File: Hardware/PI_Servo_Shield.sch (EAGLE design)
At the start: 58 parts, among them J1 RASPBERRYPI-40-PIN-GPIO, J19 QWIIC, J20 USB C, J21 Serial, U1 PCA9685, U2 PCA9306, U3 CH340C

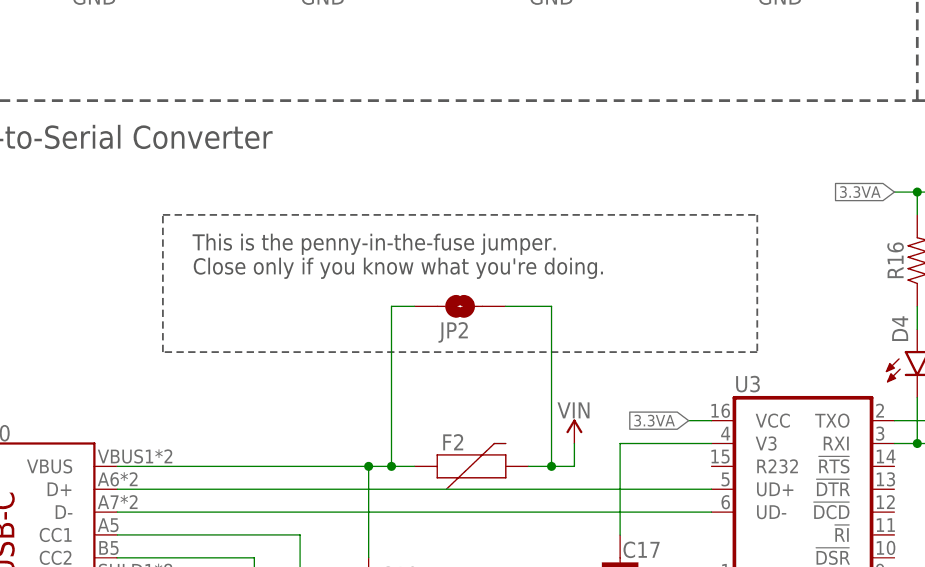
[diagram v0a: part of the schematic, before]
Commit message: adjusted I2C pullup and label
modified sch note for bypass fuse jumper
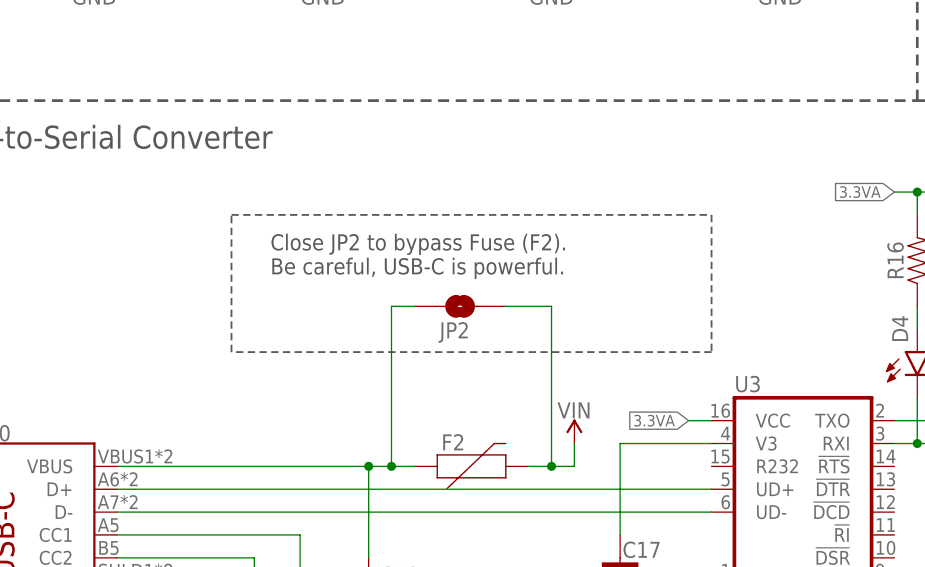
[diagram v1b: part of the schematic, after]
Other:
- note added: "Close JP2 to bypass Fuse (F2). Be careful, USB-C is powerful."
- note removed: "This is the penny-in-the-fuse jumper. Close only if you know what you're doing."
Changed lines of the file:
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@@
 <grid distance="0.1" unitdist="inch" unit="inch" style="lines" multiple="1" display="no" altdistance="0.01" altunitdist="inch" altunit="inch"/>
 <layers>
-<layer number="1" name="Top" color="4" fill="1" visible="yes" active="no"/>
-<layer number="2" name="Route2" color="1" fill="3" visible="yes" active="no"/>
-<layer number="3" name="Route3" color="4" fill="3" visible="yes" active="no"/>
-<layer number="4" name="Route4" color="1" fill="4" visible="yes" active="no"/>
-<layer number="5" name="Route5" color="4" fill="4" visible="yes" active="no"/>
-<layer number="6" name="Route6" color="1" fill="8" visible="yes" active="no"/>
-<layer number="7" name="Route7" color="4" fill="8" visible="yes" active="no"/>
-<layer number="8" name="Route8" color="1" fill="2" visible="yes" active="no"/>
-<layer number="9" name="Route9" color="4" fill="2" visible="yes" active="no"/>
-<layer number="10" name="Route10" color="1" fill="7" visible="yes" active="no"/>
-<layer number="11" name="Route11" color="4" fill="7" visible="yes" active="no"/>
-<layer number="12" name="Route12" color="1" fill="5" visible="yes" active="no"/>
-<layer number="13" name="Route13" color="4" fill="5" visible="yes" active="no"/>
-<layer number="14" name="Route14" color="1" fill="6" visible="yes" active="no"/>
-<layer number="15" name="Route15" color="4" fill="6" visible="yes" active="no"/>
-<layer number="16" name="Bottom" color="1" fill="1" visible="yes" active="no"/>
-<layer number="17" name="Pads" color="2" fill="1" visible="yes" active="no"/>
-<layer number="18" name="Vias" color="2" fill="1" visible="yes" active="no"/>
-<layer number="19" name="Unrouted" color="6" fill="1" visible="yes" active="no"/>
-<layer number="20" name="Dimension" color="15" fill="1" visible="yes" active="no"/>
-<layer number="21" name="tPlace" color="16" fill="1" visible="yes" active="no"/>
-<layer number="22" name="bPlace" color="14" fill="1" visible="yes" active="no"/>
-<layer number="23" name="tOrigins" color="15" fill="1" visible="yes" active="no"/>
-<layer number="24" name="bOrigins" color="15" fill="1" visible="yes" active="no"/>
-<layer number="25" name="tNames" color="7" fill="1" visible="yes" active="no"/>
-<layer number="26" name="bNames" color="7" fill="1" visible="yes" active="no"/>
-<layer number="27" name="tValues" color="7" fill="1" visible="yes" active="no"/>
-<layer number="28" name="bValues" color="7" fill="1" visible="yes" active="no"/>
+<layer number="1" name="Top" color="4" fill="1" visible="no" active="no"/>
+<layer number="2" name="Route2" color="1" fill="3" visible="no" active="no"/>
+<layer number="3" name="Route3" color="4" fill="3" visible="no" active="no"/>
+<layer number="4" name="Route4" color="1" fill="4" visible="no" active="no"/>
+<layer number="5" name="Route5" color="4" fill="4" visible="no" active="no"/>
+<layer number="6" name="Route6" color="1" fill="8" visible="no" active="no"/>
+<layer number="7" name="Route7" color="4" fill="8" visible="no" active="no"/>
+<layer number="8" name="Route8" color="1" fill="2" visible="no" active="no"/>
+<layer number="9" name="Route9" color="4" fill="2" visible="no" active="no"/>
+<layer number="10" name="Route10" color="1" fill="7" visible="no" active="no"/>
+<layer number="11" name="Route11" color="4" fill="7" visible="no" active="no"/>
+<layer number="12" name="Route12" color="1" fill="5" visible="no" active="no"/>
+<layer number="13" name="Route13" color="4" fill="5" visible="no" active="no"/>
+<layer number="14" name="Route14" color="1" fill="6" visible="no" active="no"/>
+<layer number="15" name="Route15" color="4" fill="6" visible="no" active="no"/>
+<layer number="16" name="Bottom" color="1" fill="1" visible="no" active="no"/>
+<layer number="17" name="Pads" color="2" fill="1" visible="no" active="no"/>
+<layer number="18" name="Vias" color="2" fill="1" visible="no" active="no"/>
+<layer number="19" name="Unrouted" color="6" fill="1" visible="no" active="no"/>
+<layer number="20" name="Dimension" color="15" fill="1" visible="no" active="no"/>
+<layer number="21" name="tPlace" color="16" fill="1" visible="no" active="no"/>
+<layer number="22" name="bPlace" color="14" fill="1" visible="no" active="no"/>
+<layer number="23" name="tOrigins" color="15" fill="1" visible="no" active="no"/>
+<layer number="24" name="bOrigins" color="15" fill="1" visible="no" active="no"/>
+<layer number="25" name="tNames" color="7" fill="1" visible="no" active="no"/>
+<layer number="26" name="bNames" color="7" fill="1" visible="no" active="no"/>
+<layer number="27" name="tValues" color="7" fill="1" visible="no" active="no"/>
+<layer number="28" name="bValues" color="7" fill="1" visible="no" active="no"/>
 <layer number="29" name="tStop" color="7" fill="3" visible="no" active="no"/>
 <layer number="30" name="bStop" color="7" fill="6" visible="no" active="no"/>
@@
 <layer number="35" name="tGlue" color="7" fill="4" visible="no" active="no"/>
 <layer number="36" name="bGlue" color="7" fill="5" visible="no" active="no"/>
-<layer number="37" name="tTest" color="7" fill="1" visible="yes" active="no"/>
-<layer number="38" name="bTest" color="7" fill="1" visible="yes" active="no"/>
+<layer number="37" name="tTest" color="7" fill="1" visible="no" active="no"/>
+<layer number="38" name="bTest" color="7" fill="1" visible="no" active="no"/>
 <layer number="39" name="tKeepout" color="4" fill="11" visible="no" active="no"/>
 <layer number="40" name="bKeepout" color="1" fill="11" visible="no" active="no"/>
@@
 <layer number="44" name="Drills" color="7" fill="1" visible="no" active="no"/>
 <layer number="45" name="Holes" color="7" fill="1" visible="no" active="no"/>
-<layer number="46" name="Milling" color="3" fill="1" visible="yes" active="no"/>
-<layer number="47" name="Measures" color="7" fill="1" visible="yes" active="no"/>
-<layer number="48" name="Document" color="7" fill="1" visible="yes" active="no"/>
-<layer number="49" name="Reference" color="7" fill="1" visible="yes" active="no"/>
-<layer number="50" name="dxf" color="7" fill="1" visible="yes" active="no"/>
-<layer number="51" name="tDocu" color="6" fill="1" visible="yes" active="no"/>
-<layer number="52" name="bDocu" color="7" fill="1" visible="yes" active="no"/>
-<layer number="53" name="tGND_GNDA" color="7" fill="9" visible="yes" active="no"/>
-<layer number="54" name="bGND_GNDA" color="1" fill="9" visible="yes" active="no"/>
-<layer number="56" name="wert" color="7" fill="1" visible="yes" active="no"/>
-<layer number="57" name="tCAD" color="7" fill="1" visible="yes" active="no"/>
-<layer number="59" name="tCarbon" color="7" fill="1" visible="yes" active="no"/>
-<layer number="60" name="bCarbon" color="7" fill="1" visible="yes" active="no"/>
+<layer number="46" name="Milling" color="3" fill="1" visible="no" active="no"/>
+<layer number="47" name="Measures" color="7" fill="1" visible="no" active="no"/>
+<layer number="48" name="Document" color="7" fill="1" visible="no" active="no"/>
+<layer number="49" name="Reference" color="7" fill="1" visible="no" active="no"/>
+<layer number="50" name="dxf" color="7" fill="1" visible="no" active="no"/>
+<layer number="51" name="tDocu" color="6" fill="1" visible="no" active="no"/>
+<layer number="52" name="bDocu" color="7" fill="1" visible="no" active="no"/>
+<layer number="53" name="tGND_GNDA" color="7" fill="9" visible="no" active="no"/>
+<layer number="54" name="bGND_GNDA" color="1" fill="9" visible="no" active="no"/>
+<layer number="56" name="wert" color="7" fill="1" visible="no" active="no"/>
+<layer number="57" name="tCAD" color="7" fill="1" visible="no" active="no"/>
+<layer number="59" name="tCarbon" color="7" fill="1" visible="no" active="no"/>
+<layer number="60" name="bCarbon" color="7" fill="1" visible="no" active="no"/>
 <layer number="88" name="SimResults" color="9" fill="1" visible="no" active="yes"/>
 <layer number="89" name="SimProbes" color="9" fill="1" visible="no" active="yes"/>
@@
 <text x="174.498" y="6.858" size="2.54" layer="94" font="vector">Pete Lewis</text>
 <text x="2.794" y="96.266" size="2.54" layer="97" font="vector">USB-to-Serial Converter</text>
-<text x="31.242" y="82.296" size="1.778" layer="97" font="vector">This is the penny-in-the-fuse jumper.
-Close only if you know what you're doing.</text>
-<wire x1="93.98" y1="73.66" x2="27.94" y2="73.66" width="0.2032" layer="97" style="shortdash"/>
-<wire x1="27.94" y1="73.66" x2="27.94" y2="88.9" width="0.2032" layer="97" style="shortdash"/>
-<wire x1="27.94" y1="88.9" x2="93.98" y2="88.9" width="0.2032" layer="97" style="shortdash"/>
-<wire x1="93.98" y1="88.9" x2="93.98" y2="73.66" width="0.2032" layer="97" style="shortdash"/>
+<text x="39.878" y="82.296" size="1.778" layer="97" font="vector">Close JP2 to bypass Fuse (F2).
+Be careful, USB-C is powerful.</text>
+<wire x1="88.9" y1="73.66" x2="35.56" y2="73.66" width="0.2032" layer="97" style="shortdash"/>
+<wire x1="35.56" y1="73.66" x2="35.56" y2="88.9" width="0.2032" layer="97" style="shortdash"/>
+<wire x1="35.56" y1="88.9" x2="88.9" y2="88.9" width="0.2032" layer="97" style="shortdash"/>
+<wire x1="88.9" y1="88.9" x2="88.9" y2="73.66" width="0.2032" layer="97" style="shortdash"/>
 <wire x1="210.82" y1="116.84" x2="210.82" y2="35.56" width="0.3048" layer="97" style="longdash"/>
 </plain>

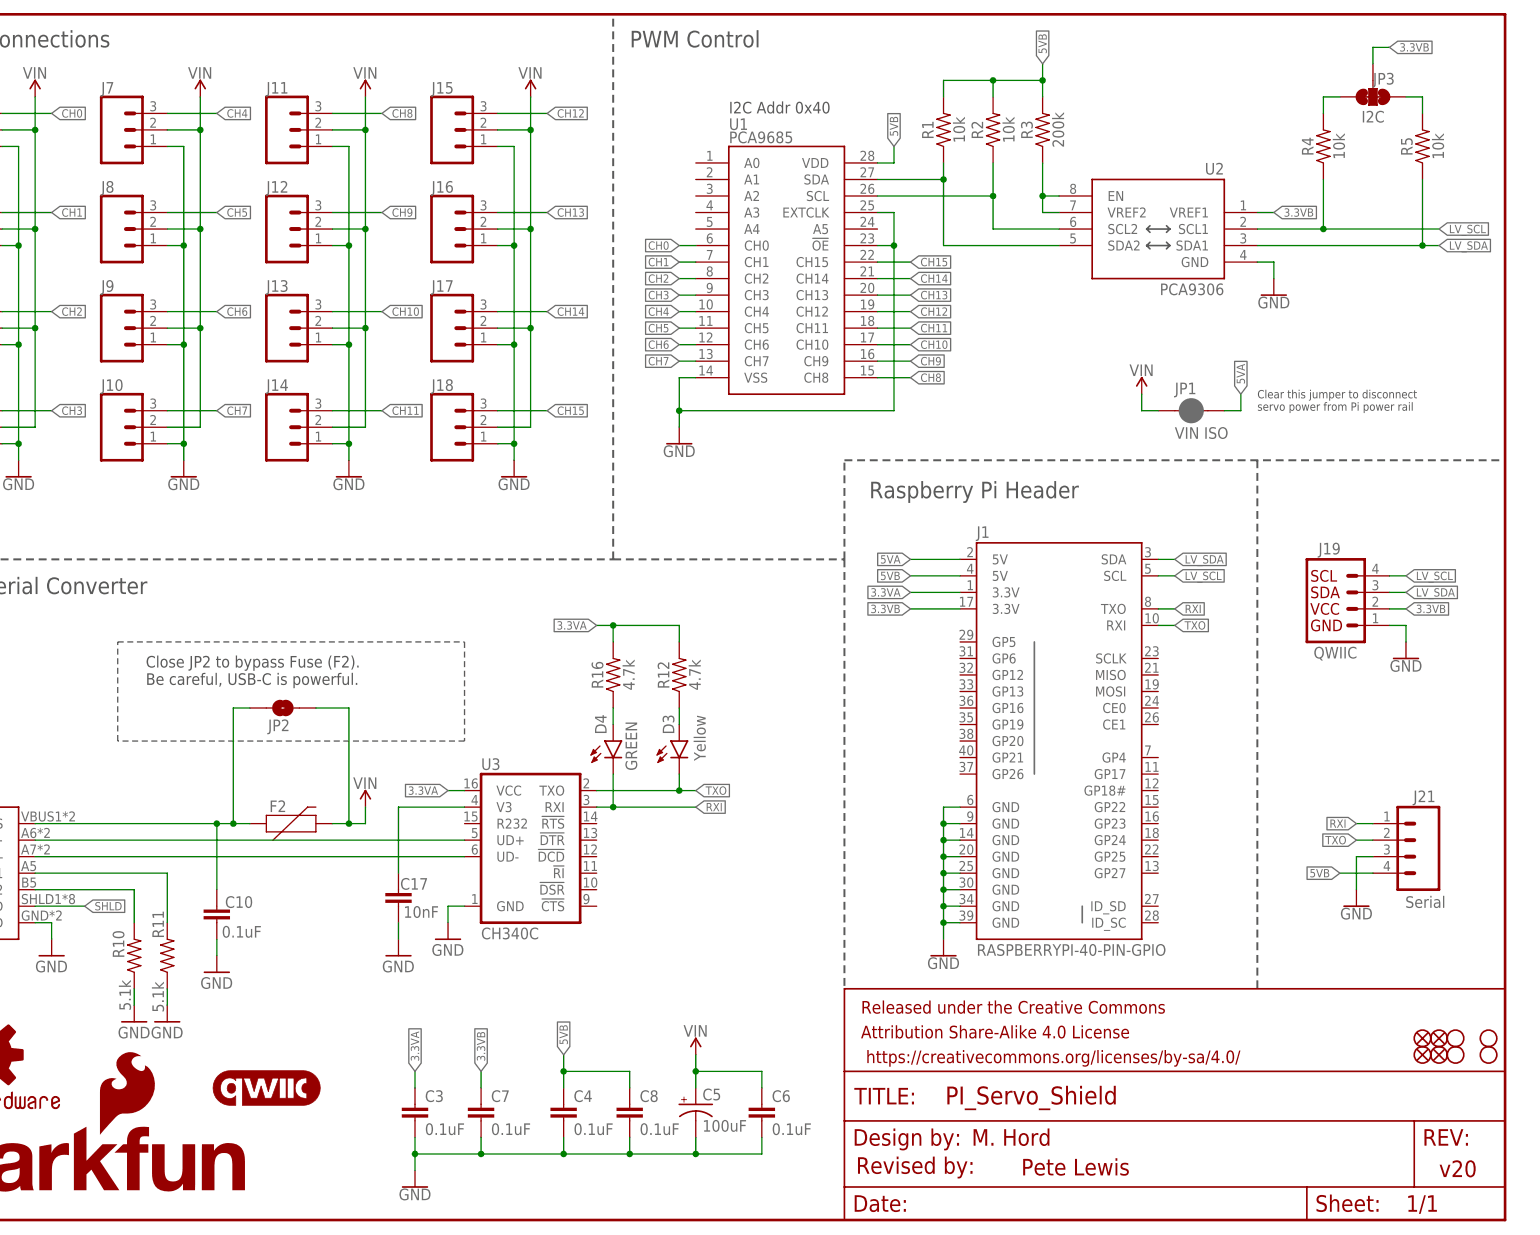
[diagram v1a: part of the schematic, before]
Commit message: post proto-design-review
SCH cleanup:
-3.3VA and 3.3VB combined into a single net and changed to arrow power symbol
-5VA and 5VB combined into a single net and changed to arrow power symbol
-added note about serial connector mating with sphero RVR
-version to v11, will jump to v20 when going to reds

BRD:
-VIN ISO juper to trace closed.
-Product Name silk updated to include "V2"
-changed "PWR" servo rail labels to "5V"
-corrected RX/TX swap, updated silk to RXI and TXO
-JP2 label changed to "FUSE BP"
-Increased 5V trace to 35 mils on connection from RVR serial header to Pi 5V pins.
-changed version in copper to v11
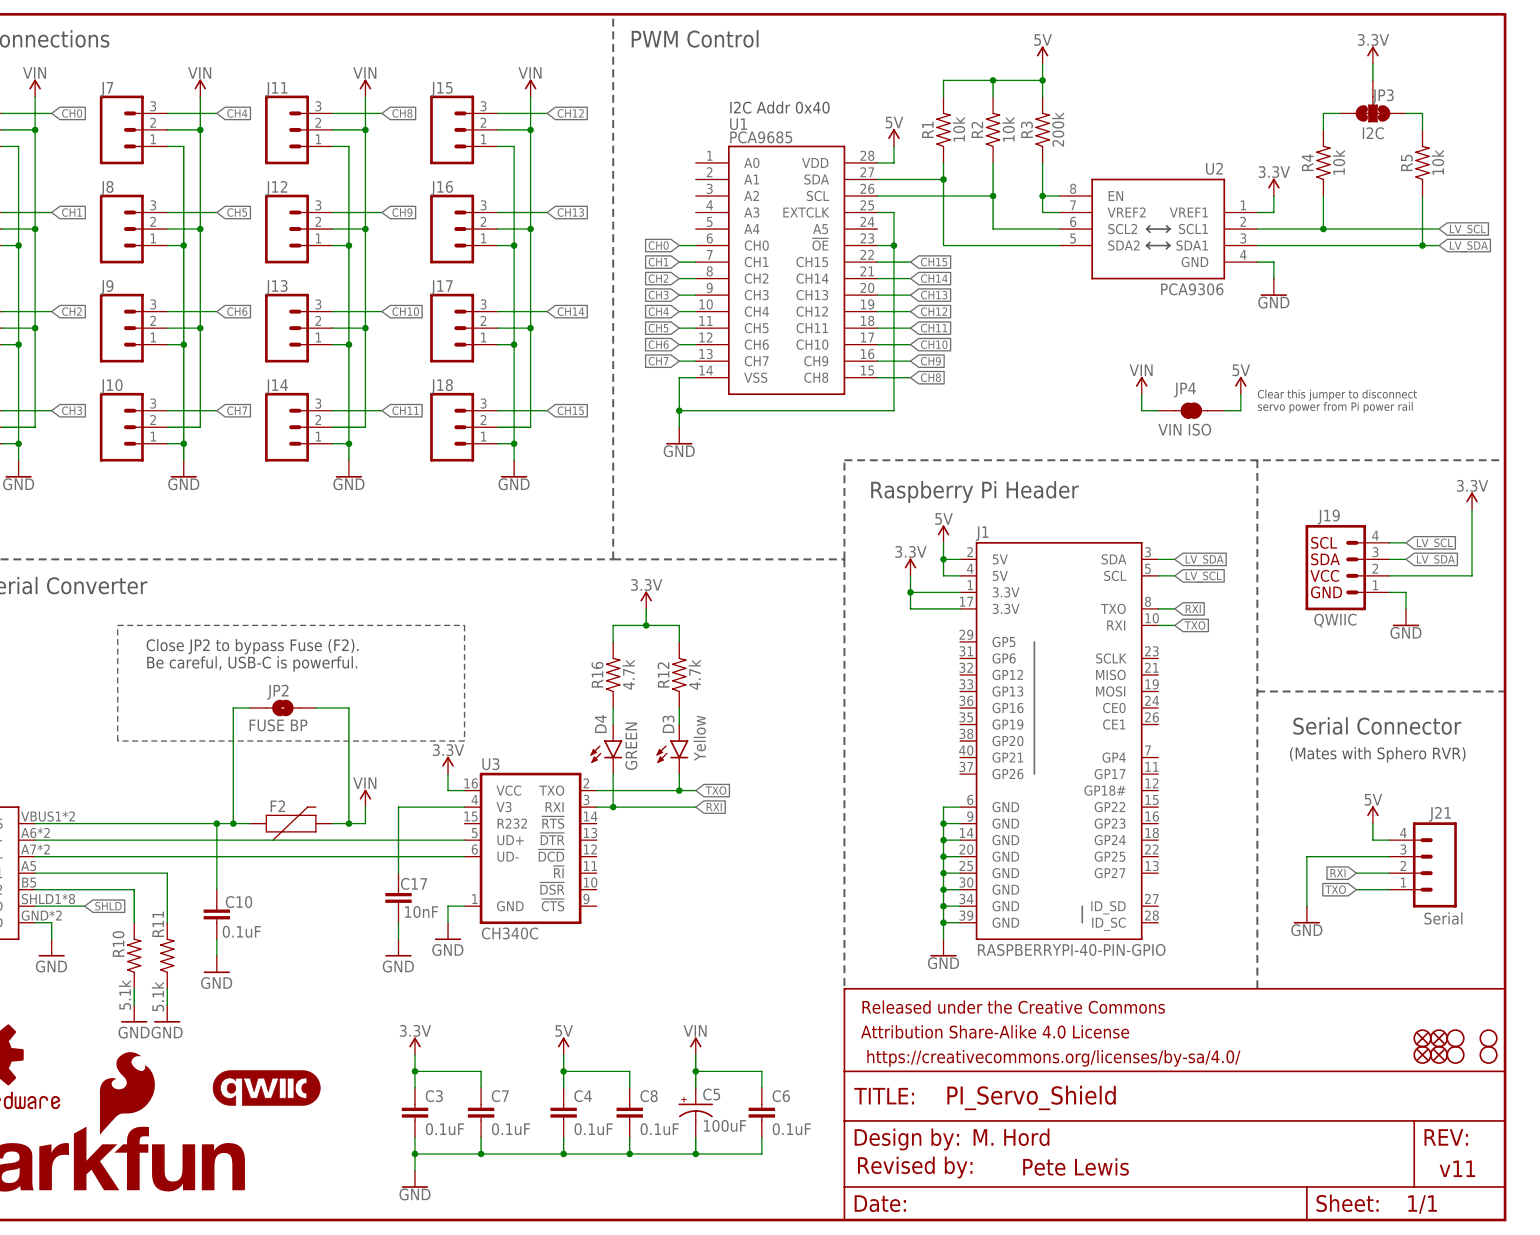
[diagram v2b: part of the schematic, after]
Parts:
- removed JP1: VIN ISO, SparkFun-Jumpers:JUMPER-SMT_2_NC_PASTE_SILK
- added JP4: VIN ISO, SparkFun-Jumpers:JUMPER-SMT_2_NC_TRACE_SILK
- JP2: value JUMPER-SMT_2_NO_SILK -> FUSE BP
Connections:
- removed net 3.3VA: C3.1, J1.3.3V@1, R12.2, R16.2, U3.VCC
- removed net 3.3VB: C7.1, J1.3.3V@17, J19.2, JP3.2, U2.VREF1
- removed net 5VA: J1.5V@2, JP1.2
- removed net 5VB: C4.1, C8.1, J1.5V@4, J21.4, R1.2, R2.2, R3.2, U1.VDD
- new net 3.3V: C3.1, C7.1, J1.3.3V@1, J1.3.3V@17, J19.2, JP3.2, R12.2, R16.2, U2.VREF1, U3.VCC
- new net 5V: C4.1, C8.1, J1.5V@2, J1.5V@4, J21.4, JP4.2, R1.2, R2.2, R3.2, U1.VDD
- net RXI: now also J21.2; no longer J21.1
- net TXO: now also J21.1; no longer J21.2
- net VIN: now also JP4.1; no longer JP1.1
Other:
- note added: "(Mates with Sphero RVR)"
- note added: "Serial Connector"
- note added: "v11"
- note removed: "v20"
- moved on the sheet: J19, J21, JP3, R4, R5
